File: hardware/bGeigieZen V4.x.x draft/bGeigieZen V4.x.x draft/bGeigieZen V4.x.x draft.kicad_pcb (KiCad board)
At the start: 2 copper layers, 129.4 x 64.6 mm, 14 parts, among them J1 M5 2x15 pin, J2 Geiger IRover, J3 GPS, J4 Geiger Safepulse, J5 Extra support header, J6 Grove

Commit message: Updated V4.0.3 boards
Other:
- board text added: "screws for the display are M3 15mm"
- board text removed: "screws for the display are M3 12mm"
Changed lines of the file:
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@@
 		)
 	)
-	(gr_text "screws for the display are M3 12mm"
+	(gr_text "screws for the display are M3 15mm"
 		(at 106.7816 141.426 0)
 		(layer "Dwgs.User")

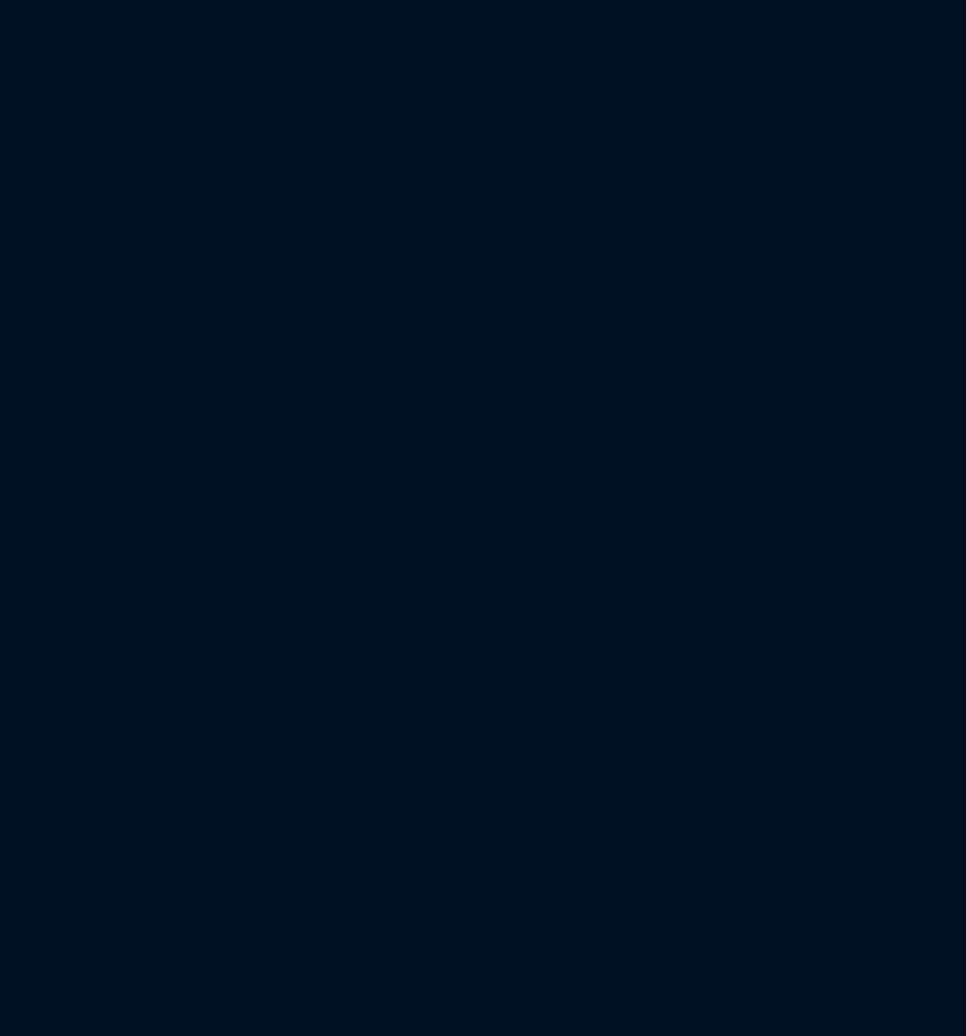
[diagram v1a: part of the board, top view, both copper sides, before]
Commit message: Changed the 18650 battery holder to a 1043 Keystone and modified the layout.
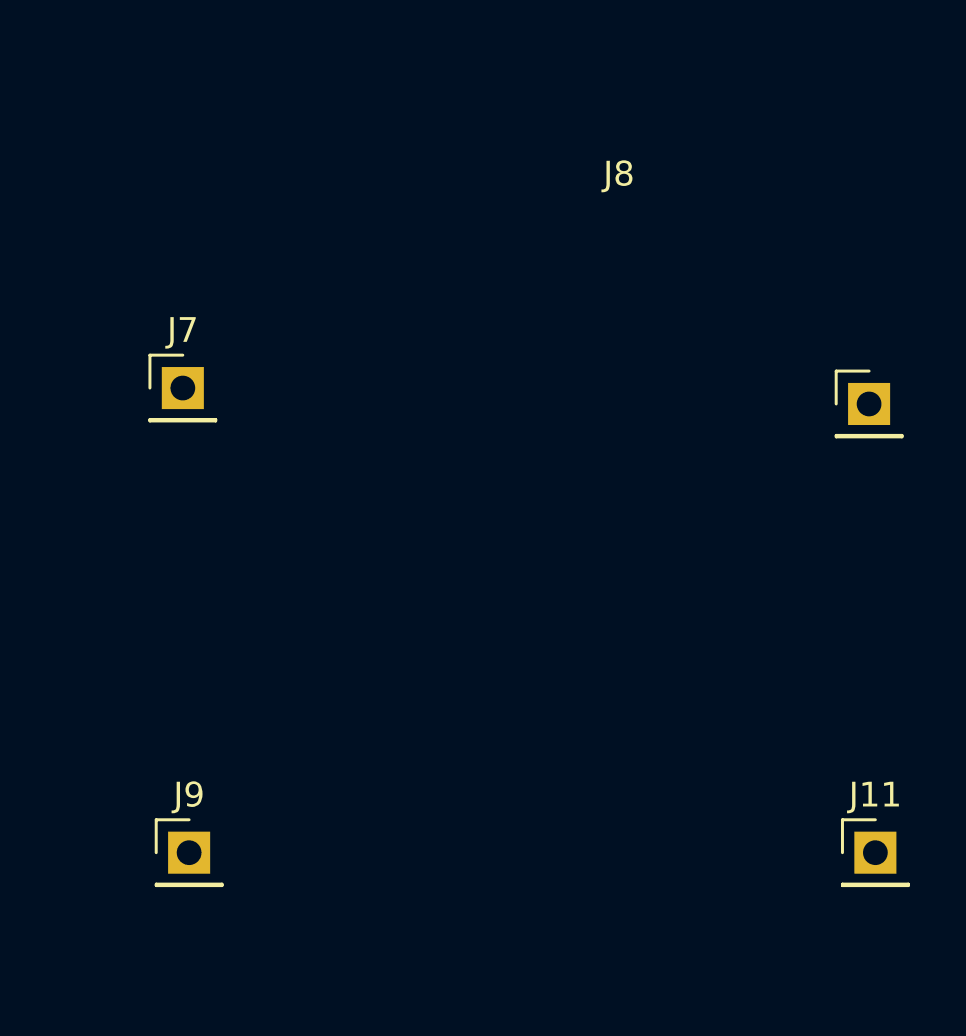
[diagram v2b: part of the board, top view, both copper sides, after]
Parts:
- removed G*** (x2): LOGO, bGeigieRaku_M5_1015:18650 map
- added J11: QI input +5V, Connector_PinHeader_2.54mm:PinHeader_1x01_P2.54mm_Vertical, F.Cu at (266.1, 104.3)
- added J7: QI GND out, Connector_PinHeader_2.54mm:PinHeader_1x01_P2.54mm_Vertical, F.Cu at (238.1, 85.6)
- added J8: QI input GND, Connector_PinHeader_2.54mm:PinHeader_1x01_P2.54mm_Vertical, F.Cu at (265.8, 86.2)
- added J9: QI battery out, Connector_PinHeader_2.54mm:PinHeader_1x01_P2.54mm_Vertical, F.Cu at (238.4, 104.3)
